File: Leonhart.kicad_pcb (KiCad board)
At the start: 8 copper layers, 410 parts, among them J1001 TC2050, J1002 Conn_01x03_Pin, J2001 TC2050, J2002 Conn_01x06_Pin, J2003 SMA-KWE901, J3002 TC2050, J3003 Conn_01x06_Pin, J3004 SMA-KWE901, J7001 USB_C_Receptacle_USB2.0_16P, J7002 USB_A, J7003 Micro_SD_Card_Det1, Q6001 DMG1012T, Q6002 DMG1012T, U1001 AM6231ASGGGAALW, U1002 SN74LVC2G241DCUR, U1003 AT24C32D-STUM-T, U2001 CC2652PSIP, U3001 nRF52840, U4001 TPS6521903RHBR, U4002 TLV62595DMQR, U5001 K4AAG165WA-BCWE, U6001 HR911130A, U6002 RTL8211F-CG, U7001 TVS0500DRVR, U7002 EMMC16G-TB29-PZ90, U7004 TPD3S014, U7005 TPS22918DBVR, X1001 32.768kHz, X1002 25MHz, X3001 32.768kHz, X3002 25MHz, X6001 ECS-2520MV-250-BN-TR

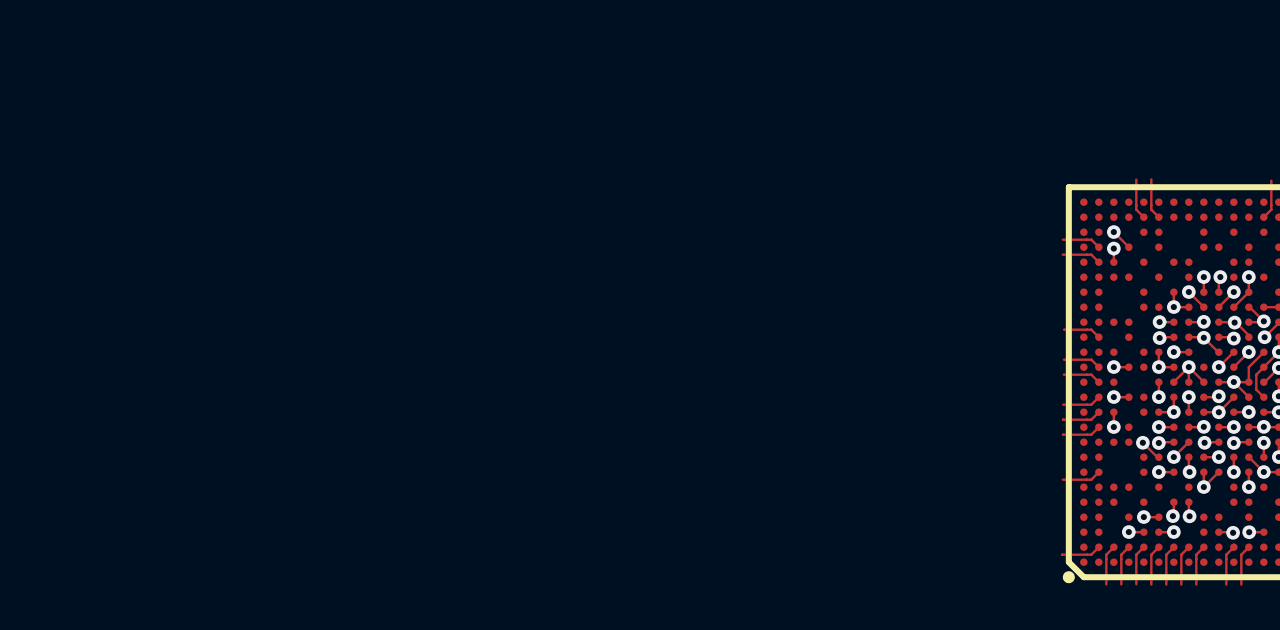
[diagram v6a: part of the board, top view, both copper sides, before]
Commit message: Added necessary nRF52840 SPI logic circuitry and GPIOs. Also added pinmux
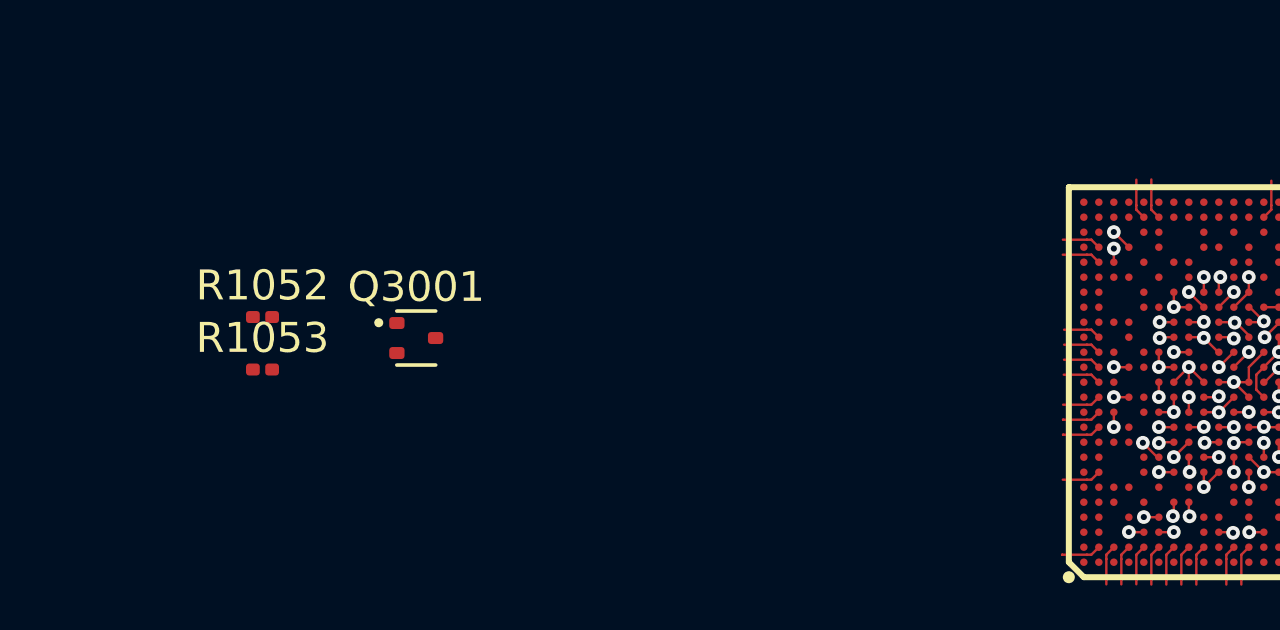
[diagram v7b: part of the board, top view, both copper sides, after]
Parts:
- added Q3001: DMG1012T, Package_TO_SOT_SMD:SOT-523, F.Cu at (120.5, 129.6)
- added R1052: 33R, Resistor_SMD:R_0201_0603Metric, F.Cu at (115.4, 128.9)
- added R1053: 33R, Resistor_SMD:R_0201_0603Metric, F.Cu at (115.4, 130.7)
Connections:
- U1001 pad A14: nRF_SPI0_CLK -> /Host System [1]/nRF_SoC_CLK
- U1001 pad A15: unconnected-(U1001R-UART0_CTSN-PadA15) -> nRF_INTn
- U1001 pad B14: nRF_SPI0_MOSI -> /Host System [1]/nRF_SoC_MOSI
- U1001 pad B15: unconnected-(U1001R-UART0_RTSN-PadB15) -> /Host System [1]/nRF_SoC_nRESET
- U3001 pad AD10: nRF_SPI0_MISO -> Net-(U3001-P0.15)
- U3001 pad Y23: unconnected-(U3001-P1.01-PadY23) -> Net-(U3001-P1.01)
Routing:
- net nRF_SPI0_MOSI: track 1.26 -> 0.00 mm
- net /Host System [1]/nRF_SoC_MOSI: track 0.00 -> 1.26 mm
- net /Host System [1]/nRF_SoC_nRESET: track 0.00 -> 1.26 mm

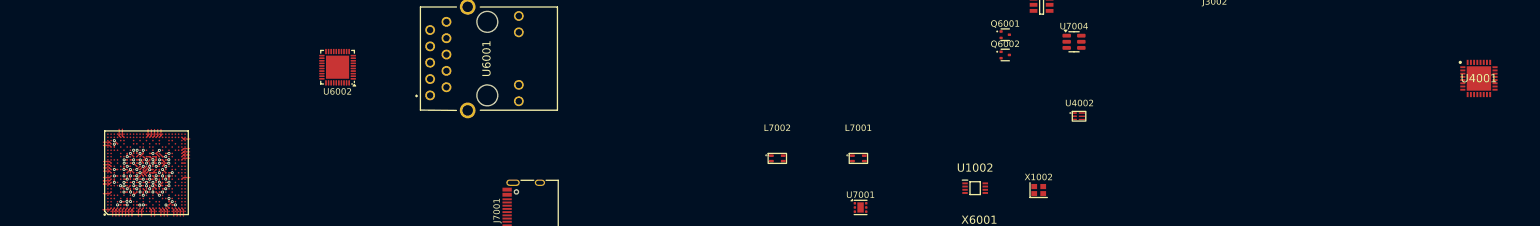
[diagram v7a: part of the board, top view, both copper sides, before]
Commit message: More SoC fanout
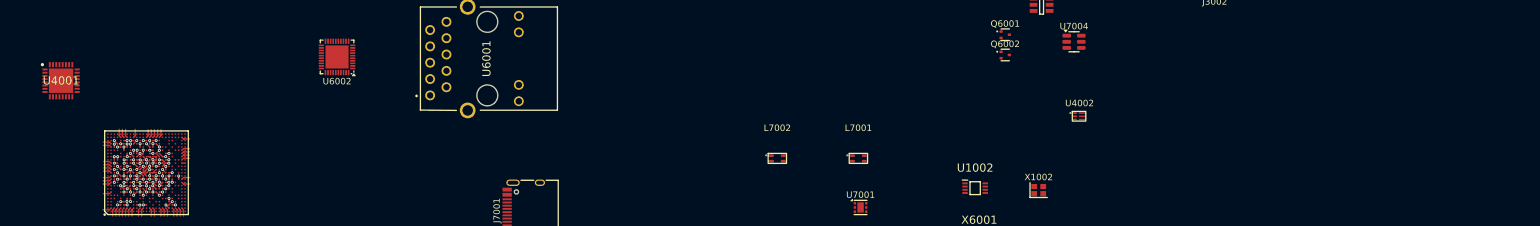
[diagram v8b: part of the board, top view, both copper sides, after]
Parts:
- moved U4001 220.4 mm to (135.5, 116.8)
- moved U6002 1.60 mm to (178.4, 113.1)
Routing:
- net UART5_CTSn: track 0.00 -> 1.35 mm
- net /USB and SD [7]/USB1_DN: track 0.00 -> 1.35 mm
- net SD_PWR_EN: track 0.00 -> 1.35 mm
- net GND: track 24.4 -> 25.4 mm, vias 19 -> 21
- net /Host System [1]/BOOTMODE12: track 0.00 -> 0.71 mm, vias 0 -> 1
- net CC2652_UART6_CTSn: track 0.00 -> 0.71 mm, vias 0 -> 1
- net /Host System [1]/UART0_TXD: track 0.00 -> 0.71 mm, vias 0 -> 1
- net /Host System [1]/BOOTMODE6: track 0.00 -> 0.70 mm, vias 0 -> 1
- net /Host System [1]/SOC_EMU0: track 0.00 -> 0.70 mm, vias 0 -> 1
- net /Host System [1]/BOOTMODE11: track 0.00 -> 0.52 mm, vias 0 -> 1
- net PORz_OUT: track 0.00 -> 0.51 mm, vias 0 -> 1
- net ETH_INTn: track 0.00 -> 0.51 mm, vias 0 -> 1
- net /Host System [1]/BOOTMODE7: track 0.00 -> 0.51 mm, vias 0 -> 1
- net RESETSTATz: track 0.00 -> 0.51 mm, vias 0 -> 1
- net /Host System [1]/BOOTMODE5: track 0.00 -> 0.50 mm, vias 0 -> 1
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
